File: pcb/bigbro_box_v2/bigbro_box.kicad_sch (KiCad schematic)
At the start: 41 parts, among them J1 Current Sense, J2 Display, J3 Mains, J4 Debug, J5 RFID, J6 Relay, K1 G5LE-1, Q1 MMBT3904, Q2 MMBT3904, Q3 BSS138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

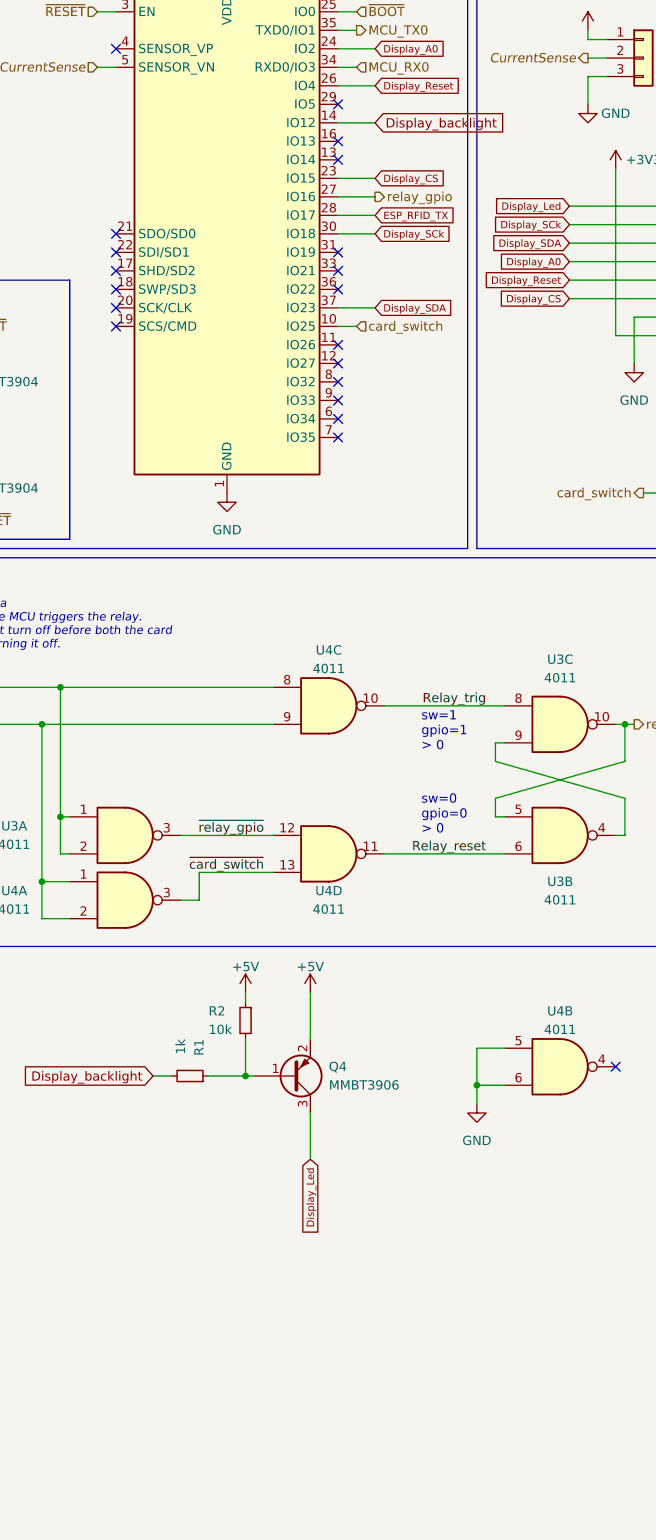
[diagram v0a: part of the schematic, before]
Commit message: Add extension connector.
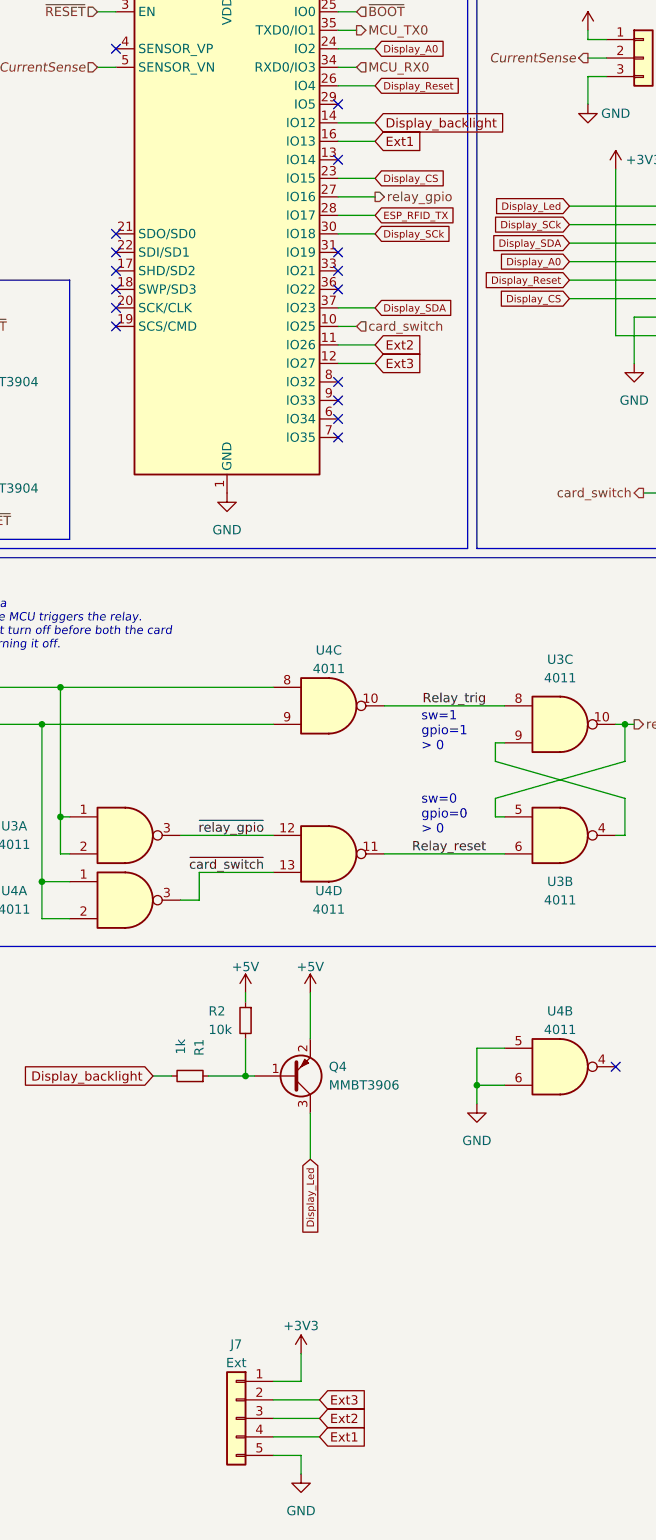
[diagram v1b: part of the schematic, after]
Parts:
- added J7: Ext, Connector_PinHeader_2.54mm:PinHeader_1x05_P2.54mm_Vertical, symbol Connector_Generic:Conn_01x05
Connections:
- net +3V3: now also J7.1 (Pin_1)
- net GND: now also J7.5 (Pin_5)
- net Ext2: now reaches U1.11 (IO26)
- net Ext2: now also J7.3 (Pin_3)
- net Ext3: now reaches U1.12 (IO27)
- net Ext3: now also J7.2 (Pin_2)
- net Ext1: now reaches U1.16 (IO13)
- net Ext1: now also J7.4 (Pin_4)
- no-connect marks 23 -> 20
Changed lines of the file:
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@@
   )
   (no_connect (at 88.9 49.53))
-  (no_connect (at 88.9 46.99))
   (no_connect (at 88.9 64.77))
   (no_connect (at 58.42 59.69))
@@
   (no_connect (at 88.9 41.91))
   (no_connect (at 58.42 34.29))
-  (no_connect (at 88.9 77.47))
   (no_connect (at 88.9 67.31))
   (no_connect (at 127 173.99))
-  (no_connect (at 88.9 74.93))
   (no_connect (at 88.9 62.23))
   (no_connect (at 88.9 82.55))
@@
     (stroke (width 0) (type default))
   )
+  (wire (pts (xy 83.82 213.36) (xy 83.82 217.17))
+    (stroke (width 0) (type default))
+  )
   (wire (pts (xy 127 73.66) (xy 134.62 73.66))
     (stroke (width 0) (type default))
@@
     (stroke (width 0) (type default))
   )
+  (wire (pts (xy 88.9 77.47) (xy 93.98 77.47))
+    (stroke (width 0) (type default))
+  )
   (wire (pts (xy 377.19 48.26) (xy 377.19 49.53))
     (stroke (width 0) (type default))
@@
     (stroke (width 0) (type default))
   )
+  (wire (pts (xy 83.82 227.33) (xy 83.82 229.87))
+    (stroke (width 0) (type default))
+  )
   (wire (pts (xy 334.01 86.36) (xy 334.01 93.98))
     (stroke (width 0) (type default))
@@
     (stroke (width 0) (type default))
   )
+  (wire (pts (xy 80.01 227.33) (xy 83.82 227.33))
+    (stroke (width 0) (type default))
+  )
   (wire (pts (xy 120.65 58.42) (xy 134.62 58.42))
     (stroke (width 0) (type default))
@@
     (stroke (width 0) (type default))
   )
+  (wire (pts (xy 88.9 74.93) (xy 93.98 74.93))
+    (stroke (width 0) (type default))
+  )
+  (wire (pts (xy 80.01 219.71) (xy 86.36 219.71))
+    (stroke (width 0) (type default))
+  )
   (wire (pts (xy 48.26 148.59) (xy 48.26 153.67))
     (stroke (width 0) (type default))
@@
     (stroke (width 0) (type default))
   )
+  (wire (pts (xy 83.82 217.17) (xy 80.01 217.17))
+    (stroke (width 0) (type default))
+  )
   (wire (pts (xy 134.62 71.12) (xy 129.54 71.12))
     (stroke (width 0) (type default))
@@
     (stroke (width 0) (type default))
   )
+  (wire (pts (xy 88.9 46.99) (xy 93.98 46.99))
+    (stroke (width 0) (type default))
+  )
   (wire (pts (xy 50.8 139.7) (xy 50.8 144.78))
     (stroke (width 0) (type default))
@@
   )
   (wire (pts (xy 127 127) (xy 128.27 127))
+    (stroke (width 0) (type default))
+  )
+  (wire (pts (xy 80.01 222.25) (xy 86.36 222.25))
+    (stroke (width 0) (type default))
+  )
+  (wire (pts (xy 80.01 224.79) (xy 86.36 224.79))
     (stroke (width 0) (type default))
   )
@@
   (label "NC" (at 369.57 81.28 180) (fields_autoplaced)
     (effects (font (size 1.27 1.27)) (justify right bottom))
+  )
+  (global_label "Ext3" (shape input) (at 86.36 219.71 0) (fields_autoplaced)
+    (effects (font (size 1.27 1.27)) (justify left))
+    (property "Intersheetrefs" "${INTERSHEET_REFS}" (at 93.3781 219.71 0)
+      (effects (font (size 1.27 1.27)) (justify left) hide)
+    )
   )
   (global_label "Display_backlight" (shape input) (at 63.5 175.26 180) (fields_autoplaced)
@@
     )
   )
+  (global_label "Ext2" (shape input) (at 93.98 74.93 0) (fields_autoplaced)
+    (effects (font (size 1.27 1.27)) (justify left))
+    (property "Intersheetrefs" "${INTERSHEET_REFS}" (at 100.9981 74.93 0)
+      (effects (font (size 1.27 1.27)) (justify left) hide)
+    )
+  )
   (global_label "Display_CS" (shape input) (at 93.98 52.07 0) (fields_autoplaced)
     (effects (font (size 1 1)) (justify left))
@@
     )
   )
+  (global_label "Ext2" (shape input) (at 86.36 222.25 0) (fields_autoplaced)
+    (effects (font (size 1.27 1.27)) (justify left))
+    (property "Intersheetrefs" "${INTERSHEET_REFS}" (at 93.3781 222.25 0)
+      (effects (font (size 1.27 1.27)) (justify left) hide)
+    )
+  )
   (global_label "ESP_RFID_TX" (shape input) (at 194.31 40.64 0) (fields_autoplaced)
     (effects (font (size 1.27 1.27)) (justify left))
@@
     )
   )
+  (global_label "Ext1" (shape input) (at 86.36 224.79 0) (fields_autoplaced)
+    (effects (font (size 1.27 1.27)) (justify left))
+    (property "Intersheetrefs" "${INTERSHEET_REFS}" (at 93.3781 224.79 0)
+      (effects (font (size 1.27 1.27)) (justify left) hide)
+    )
+  )
   (global_label "Display_Reset" (shape input) (at 120.65 66.04 180) (fields_autoplaced)
     (effects (font (size 1 1)) (justify right))
@@
     )
   )
+  (global_label "Ext3" (shape input) (at 93.98 77.47 0) (fields_autoplaced)
+    (effects (font (size 1.27 1.27)) (justify left))
+    (property "Intersheetrefs" "${INTERSHEET_REFS}" (at 100.9981 77.47 0)
+      (effects (font (size 1.27 1.27)) (justify left) hide)
+    )
+  )
   (global_label "Display_Led" (shape input) (at 85.09 186.69 270) (fields_autoplaced)
     (effects (font (size 1 1)) (justify right))
@@
     )
   )
+  (global_label "Ext1" (shape input) (at 93.98 46.99 0) (fields_autoplaced)
+    (effects (font (size 1.27 1.27)) (justify left))
+    (property "Intersheetrefs" "${INTERSHEET_REFS}" (at 100.9981 46.99 0)
+      (effects (font (size 1.27 1.27)) (justify left) hide)
+    )
+  )
   (global_label "Display_Reset" (shape input) (at 93.98 39.37 0) (fields_autoplaced)
     (effects (font (size 1 1)) (justify left))
@@
         (path "/212a0d71-cc7b-49f8-b4ca-a935e5355dca"
           (reference "#PWR03") (unit 1)
+        )
+      )
+    )
+  )
+  (symbol (lib_id "power:GND") (at 83.82 229.87 0) (unit 1)
+    (in_bom yes) (on_board yes) (dnp no) (fields_autoplaced)
+    (property "Reference" "#PWR012" (at 83.82 236.22 0)
+      (effects (font (size 1.27 1.27)) hide)
+    )
+    (property "Value" "GND" (at 83.82 234.95 0)
+      (effects (font (size 1.27 1.27)))
+    )
+    (property "Footprint" "" (at 83.82 229.87 0)
+      (effects (font (size 1.27 1.27)) hide)
+    )
+    (property "Datasheet" "" (at 83.82 229.87 0)
+      (effects (font (size 1.27 1.27)) hide)
+    )
+    (pin "1")
+    (instances
+      (project "bigbro_box"
+        (path "/212a0d71-cc7b-49f8-b4ca-a935e5355dca"
+          (reference "#PWR012") (unit 1)
         )
       )
@@
         (path "/212a0d71-cc7b-49f8-b4ca-a935e5355dca"
           (reference "R8") (unit 1)
+        )
+      )
+    )
+  )
+  (symbol (lib_id "Connector_Generic:Conn_01x05") (at 74.93 222.25 0) (mirror y) (unit 1)
+    (in_bom yes) (on_board yes) (dnp no) (fields_autoplaced)
+    (property "Reference" "J7" (at 74.93 212.09 0)
+      (effects (font (size 1.27 1.27)))
+    )
+    (property "Value" "Ext" (at 74.93 214.63 0)
+      (effects (font (size 1.27 1.27)))
+    )
+    (property "Footprint" "Connector_PinHeader_2.54mm:PinHeader_1x05_P2.54mm_Vertical" (at 74.93 222.25 0)
+      (effects (font (size 1.27 1.27)) hide)
+    )
+    (property "Datasheet" "~" (at 74.93 222.25 0)
+      (effects (font (size 1.27 1.27)) hide)
+    )
+    (pin "1")
+    (pin "2")
+    (pin "3")
+    (pin "4")
+    (pin "5")
+    (instances
+      (project "bigbro_box"
+        (path "/212a0d71-cc7b-49f8-b4ca-a935e5355dca"
+          (reference "J7") (unit 1)
         )
       )
@@
         )
       )
+    )
+  )
+  (symbol (lib_id "power:+3V3") (at 83.82 213.36 0) (unit 1)
+    (in_bom yes) (on_board yes) (dnp no) (fields_autoplaced)
+    (property "Reference" "#PWR011" (at 83.82 217.17 0)
+      (effects (font (size 1.27 1.27)) hide)
+    )
+    (property "Value" "+3V3" (at 83.82 209.55 0)
+      (effects (font (size 1.27 1.27)))
+    )
+    (property "Footprint" "" (at 83.82 213.36 0)
+      (effects (font (size 1.27 1.27)) hide)
+    )
+    (property "Datasheet" "" (at 83.82 213.36 0)
+      (effects (font (size 1.27 1.27)) hide)
+    )
+    (pin "1")
+    (instances
+      (project "bigbro_box"
+        (path "/212a0d71-cc7b-49f8-b4ca-a935e5355dca"
+          (reference "#PWR011") (unit 1)
+        )
+      )

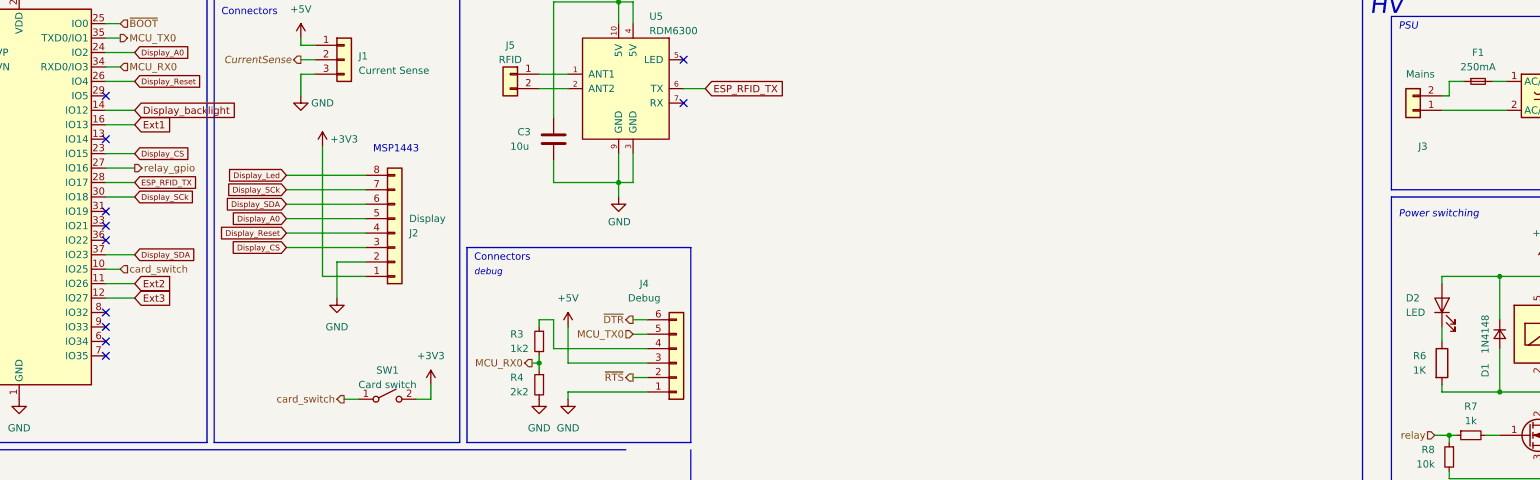
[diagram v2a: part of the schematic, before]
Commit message: Move display backlight from GPIO12 to GPIO14 to fix boot problem.
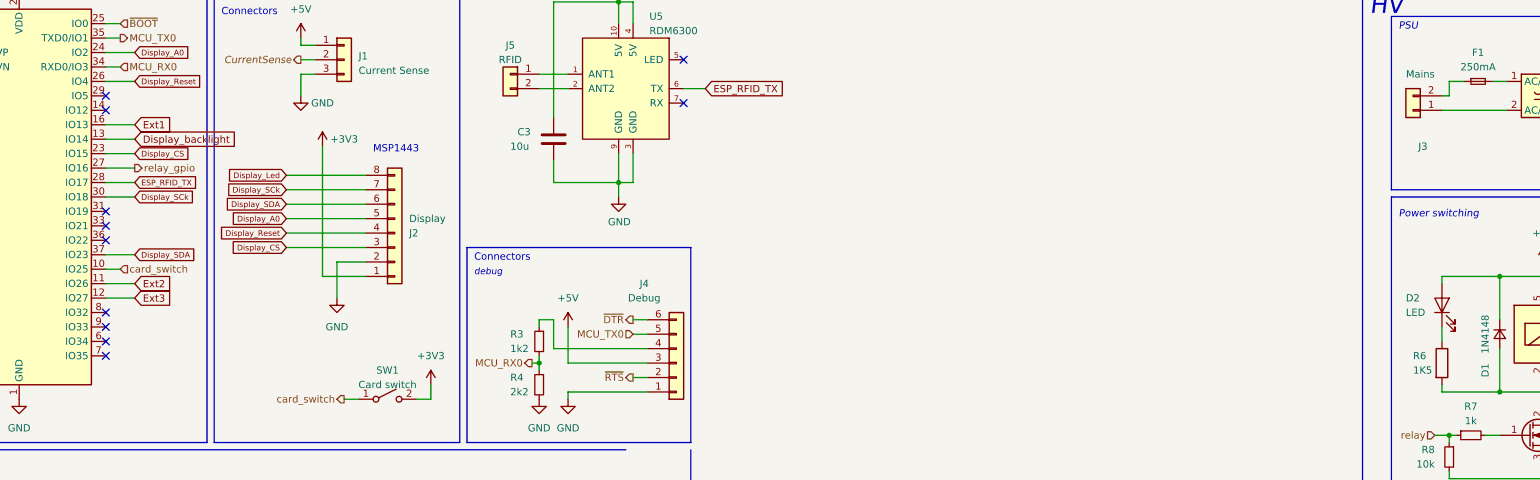
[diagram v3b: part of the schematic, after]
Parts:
- R6: value 1K -> 1K5
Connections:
- net Display_backlight: now also U1.13 (IO14); no longer U1.14 (IO12)
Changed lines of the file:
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@@
   (junction (at 149.86 121.92) (diameter 0) (color 0 0 0 0)
   )
-  (no_connect (at 88.9 49.53))
   (no_connect (at 88.9 64.77))
   (no_connect (at 58.42 59.69))
@@
   (no_connect (at 88.9 80.01))
   (no_connect (at 190.5 43.18))
+  (no_connect (at 88.9 44.45))
   (wire (pts (xy 356.87 39.37) (xy 367.03 39.37))
     (stroke (width 0) (type default))
@@
     (stroke (width 0) (type default))
   )
-  (wire (pts (xy 88.9 44.45) (xy 93.98 44.45))
-    (stroke (width 0) (type default))
-  )
   (polyline (pts (xy 309.88 22.86) (xy 309.88 119.38))
     (stroke (width 0) (type default))
@@
   )
   (wire (pts (xy 170.18 88.9) (xy 184.15 88.9))
+    (stroke (width 0) (type default))
+  )
+  (wire (pts (xy 88.9 49.53) (xy 93.98 49.53))
     (stroke (width 0) (type default))
   )
@@
     )
   )
-  (global_label "Display_backlight" (shape input) (at 93.98 44.45 0) (fields_autoplaced)
+  (global_label "Display_backlight" (shape input) (at 93.98 49.53 0) (fields_autoplaced)
     (effects (font (size 1.27 1.27)) (justify left))
-    (property "Intersheetrefs" "${INTERSHEET_REFS}" (at 112.9031 44.3706 0)
+    (property "Intersheetrefs" "${INTERSHEET_REFS}" (at 112.9031 49.4506 0)
       (effects (font (size 1.27 1.27)) (justify left) hide)
     )
@@
       (effects (font (size 1.27 1.27)) (justify left))
     )
-    (property "Value" "1K" (at 318.77 90.17 0)
-      (effects (font (size 1.27 1.27)) (justify left))
-    )
+    (property "Value" "1K5" (at 318.77 90.17 0)
+      (effects (font (size 1.27 1.27)) (justify left))
+    )
